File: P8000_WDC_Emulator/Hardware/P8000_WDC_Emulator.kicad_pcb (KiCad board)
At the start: 2 copper layers, 144 x 160.4 mm, 81 parts, among them Q1 CRYSTAL, SW1 SW_PUSH, X1 RS-232, X2 P8000, X3 SD-CON, X4 PATA, X5 4_Pin_Molex, X6 P8000-Compact, X7 AVR-ISP-6

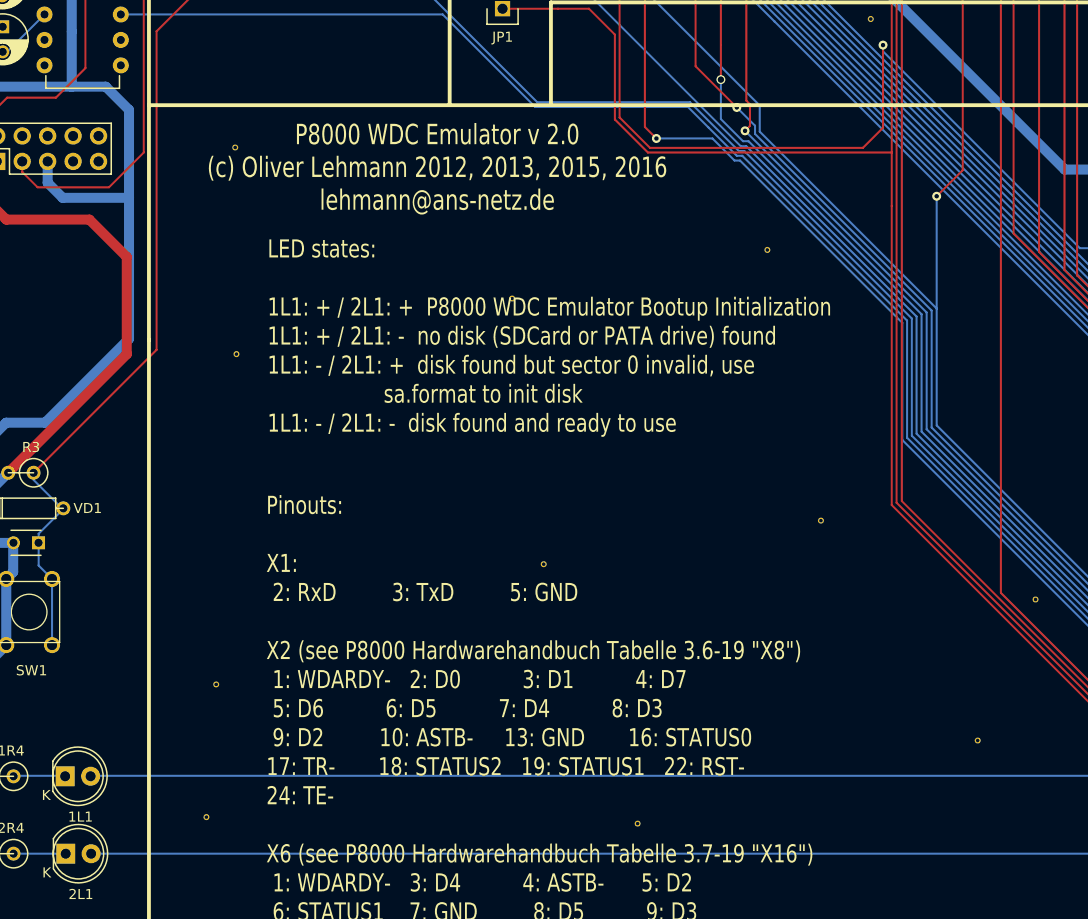
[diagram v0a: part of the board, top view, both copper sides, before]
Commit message: more ground layer
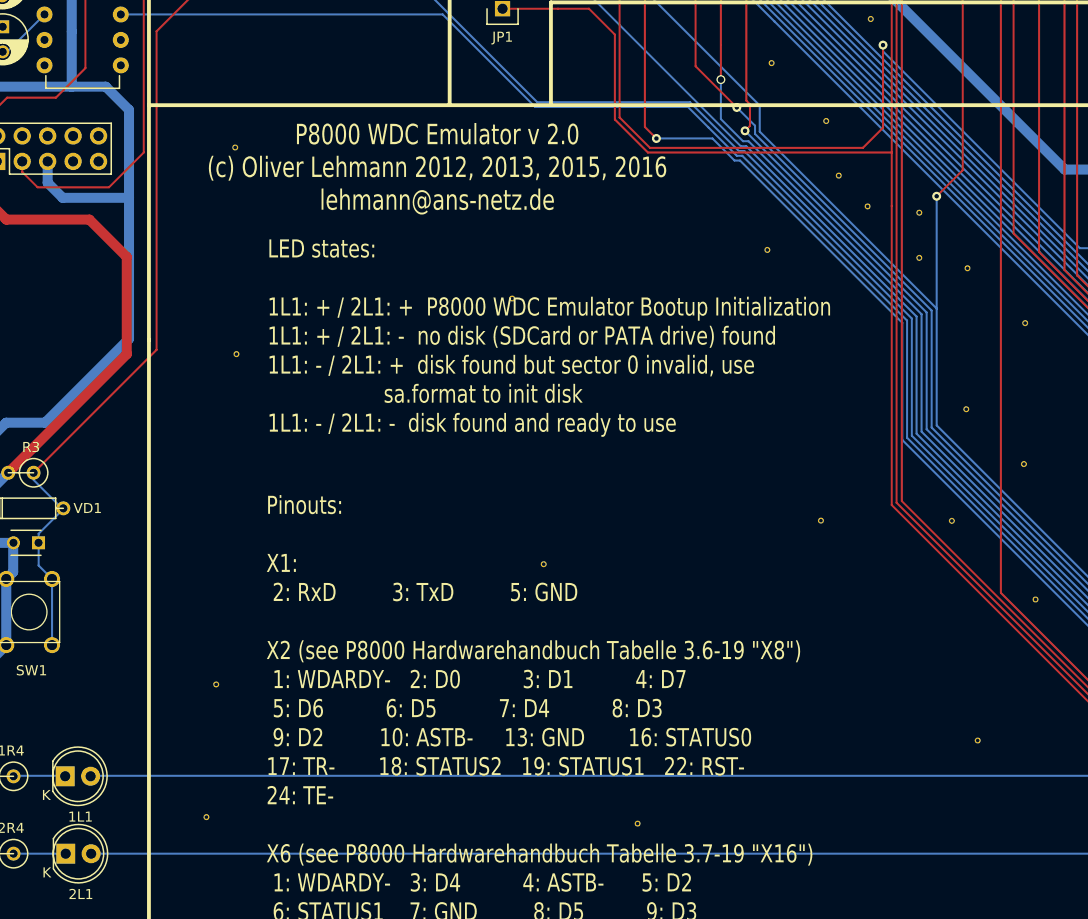
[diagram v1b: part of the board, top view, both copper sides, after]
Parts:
- added VIA-0.6mm: VAL**, Footprints:VIA-0.6mm, F.Cu at (120.6, 112.9)
- added VIA-0.6mm: VAL**, Footprints:VIA-0.6mm, F.Cu at (102.7, 67.2)
- added VIA-0.6mm: VAL**, Footprints:VIA-0.6mm, F.Cu at (109.4, 78.5)
- added VIA-0.6mm: VAL**, Footprints:VIA-0.6mm, F.Cu at (122.2, 87.7)
- added VIA-0.6mm: VAL**, Footprints:VIA-0.6mm, F.Cu at (122.1, 101.8)
- added VIA-0.6mm: VAL**, Footprints:VIA-0.6mm, F.Cu at (127.8, 107.3)
- added VIA-0.6mm: VAL**, Footprints:VIA-0.6mm, F.Cu at (128.0, 93.2)
- added VIA-0.6mm: VAL**, Footprints:VIA-0.6mm, F.Cu at (117.4, 86.7)
- added VIA-0.6mm: VAL**, Footprints:VIA-0.6mm, F.Cu at (117.4, 82.2)
- added VIA-0.6mm: VAL**, Footprints:VIA-0.6mm, F.Cu at (112.2, 81.5)
- added VIA-0.6mm: VAL**, Footprints:VIA-0.6mm, F.Cu at (108.1, 73.0)
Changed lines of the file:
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@@
 (kicad_pcb (version 4) (host pcbnew 4.0.1-stable)
   (general
-    (links 226)
+    (links 237)
     (no_connects 0)
     (area 19.428459 20.282295 164.490038 181.940201)
@@
     (tracks 1219)
     (zones 0)
-    (modules 81)
+    (modules 92)
     (nets 116)
   )
@@
     (mod_text_size 1.524 1.524)
     (mod_text_width 0.3048)
-    (pad_size 1.7272 1.7272)
+    (pad_size 1.9 1.9)
     (pad_drill 1.016)
     (pad_to_mask_clearance 0.254)
@@
     (visible_elements 7FFFFF7F)
     (pcbplotparams
-      (layerselection 0x00030_80000001)
+      (layerselection 0x010e8_80000001)
       (usegerberextensions true)
       (excludeedgelayer false)
@@
       (outputformat 1)
       (mirror false)
-      (drillshape 2)
+      (drillshape 0)
       (scaleselection 1)
       (outputdirectory PCB/))
@@
     (add_net VCC)
   )
+  (module Footprints:VIA-0.6mm (layer Front)
+    (at 120.64492 112.92332)
+    (path VIA-0.6mm)
+    (fp_text reference VIA-0.6mm (at 0 -4.445) (layer F.SilkS) hide
+      (effects (font (thickness 0.3048)))
+    )
+    (fp_text value VAL** (at 0.635 3.81) (layer F.SilkS) hide
+      (effects (font (thickness 0.3048)))
+    )
+    (pad 1 thru_hole circle (at 0 0) (size 0.59944 0.59944) (drill 0.35) (layers *.Cu)
+      (net 41 GND) (clearance 0.00254))
+  )
+  (module Footprints:VIA-0.6mm (layer Front)
+    (at 122.20702 87.7062)
+    (path VIA-0.6mm)
+    (fp_text reference VIA-0.6mm (at 0 -4.445) (layer F.SilkS) hide
+      (effects (font (thickness 0.3048)))
+    )
+    (fp_text value VAL** (at 0.635 3.81) (layer F.SilkS) hide
+      (effects (font (thickness 0.3048)))
+    )
+    (pad 1 thru_hole circle (at 0 0) (size 0.59944 0.59944) (drill 0.35) (layers *.Cu)
+      (net 41 GND) (clearance 0.00254))
+  )
+  (module Footprints:VIA-0.6mm (layer Front)
+    (at 122.08256 101.7778)
+    (path VIA-0.6mm)
+    (fp_text reference VIA-0.6mm (at 0 -4.445) (layer F.SilkS) hide
+      (effects (font (thickness 0.3048)))
+    )
+    (fp_text value VAL** (at 0.635 3.81) (layer F.SilkS) hide
+      (effects (font (thickness 0.3048)))
+    )
+    (pad 1 thru_hole circle (at 0 0) (size 0.59944 0.59944) (drill 0.35) (layers *.Cu)
+      (net 41 GND) (clearance 0.00254))
+  )
+  (module Footprints:VIA-0.6mm (layer Front)
+    (at 127.8382 107.25404)
+    (path VIA-0.6mm)
+    (fp_text reference VIA-0.6mm (at 0 -4.445) (layer F.SilkS) hide
+      (effects (font (thickness 0.3048)))
+    )
+    (fp_text value VAL** (at 0.635 3.81) (layer F.SilkS) hide
+      (effects (font (thickness 0.3048)))
+    )
+    (pad 1 thru_hole circle (at 0 0) (size 0.59944 0.59944) (drill 0.35) (layers *.Cu)
+      (net 41 GND) (clearance 0.00254))
+  )
+  (module Footprints:VIA-0.6mm (layer Front)
+    (at 127.96266 93.18244)
+    (path VIA-0.6mm)
+    (fp_text reference VIA-0.6mm (at 0 -4.445) (layer F.SilkS) hide
+      (effects (font (thickness 0.3048)))
+    )
+    (fp_text value VAL** (at 0.635 3.81) (layer F.SilkS) hide
+      (effects (font (thickness 0.3048)))
+    )
+    (pad 1 thru_hole circle (at 0 0) (size 0.59944 0.59944) (drill 0.35) (layers *.Cu)
+      (net 41 GND) (clearance 0.00254))
+  )
+  (module Footprints:VIA-0.6mm (layer Front)
+    (at 117.39372 86.66988)
+    (path VIA-0.6mm)
+    (fp_text reference VIA-0.6mm (at 0 -4.445) (layer F.SilkS) hide
+      (effects (font (thickness 0.3048)))
+    )
+    (fp_text value VAL** (at 0.635 3.81) (layer F.SilkS) hide
+      (effects (font (thickness 0.3048)))
+    )
+    (pad 1 thru_hole circle (at 0 0) (size 0.59944 0.59944) (drill 0.35) (layers *.Cu)
+      (net 41 GND) (clearance 0.00254))
+  )
+  (module Footprints:VIA-0.6mm (layer Front)
+    (at 117.39372 82.15884)
+    (path VIA-0.6mm)
+    (fp_text reference VIA-0.6mm (at 0 -4.445) (layer F.SilkS) hide
+      (effects (font (thickness 0.3048)))
+    )
+    (fp_text value VAL** (at 0.635 3.81) (layer F.SilkS) hide
+      (effects (font (thickness 0.3048)))
+    )
+    (pad 1 thru_hole circle (at 0 0) (size 0.59944 0.59944) (drill 0.35) (layers *.Cu)
+      (net 41 GND) (clearance 0.00254))
+  )
+  (module Footprints:VIA-0.6mm (layer Front)
+    (at 112.23498 81.52892)
+    (path VIA-0.6mm)
+    (fp_text reference VIA-0.6mm (at 0 -4.445) (layer F.SilkS) hide
+      (effects (font (thickness 0.3048)))
+    )
+    (fp_text value VAL** (at 0.635 3.81) (layer F.SilkS) hide
+      (effects (font (thickness 0.3048)))
+    )
+    (pad 1 thru_hole circle (at 0 0) (size 0.59944 0.59944) (drill 0.35) (layers *.Cu)
+      (net 41 GND) (clearance 0.00254))
+  )
+  (module Footprints:VIA-0.6mm (layer Front)
+    (at 108.09986 73.00722)
+    (path VIA-0.6mm)
+    (fp_text reference VIA-0.6mm (at 0 -4.445) (layer F.SilkS) hide
+      (effects (font (thickness 0.3048)))
+    )
+    (fp_text value VAL** (at 0.635 3.81) (layer F.SilkS) hide
+      (effects (font (thickness 0.3048)))
+    )
+    (pad 1 thru_hole circle (at 0 0) (size 0.59944 0.59944) (drill 0.35) (layers *.Cu)
+      (net 41 GND) (clearance 0.00254))
+  )
+  (module Footprints:VIA-0.6mm (layer Front)
+    (at 102.65156 67.22364)
+    (path VIA-0.6mm)
+    (fp_text reference VIA-0.6mm (at 0 -4.445) (layer F.SilkS) hide
+      (effects (font (thickness 0.3048)))
+    )
+    (fp_text value VAL** (at 0.635 3.81) (layer F.SilkS) hide
+      (effects (font (thickness 0.3048)))
+    )
+    (pad 1 thru_hole circle (at 0 0) (size 0.59944 0.59944) (drill 0.35) (layers *.Cu)
+      (net 41 GND) (clearance 0.00254))
+  )
+  (module Footprints:VIA-0.6mm (layer Front)
+    (at 109.35716 78.45552)
+    (path VIA-0.6mm)
+    (fp_text reference VIA-0.6mm (at 0 -4.445) (layer F.SilkS) hide
+      (effects (font (thickness 0.3048)))
+    )
+    (fp_text value VAL** (at 0.635 3.81) (layer F.SilkS) hide
+      (effects (font (thickness 0.3048)))
+    )
+    (pad 1 thru_hole circle (at 0 0) (size 0.59944 0.59944) (drill 0.35) (layers *.Cu)
+      (net 41 GND) (clearance 0.00254))
+  )
   (module TO92-LM317 (layer Front)
     (at 143.90116 73.12406 270)
@@
       (effects (font (size 1 1) (thickness 0.15)))
     )
-    (pad 1 thru_hole rect (at 0 0 90) (size 2 1.9) (drill 1.00076) (layers *.Cu *.Mask F.SilkS)
+    (pad 1 thru_hole rect (at 0 0 90) (size 2 1.9) (drill 1.016) (layers *.Cu *.Mask F.SilkS)
       (net 52 "Net-(2L1-Pad1)"))
-    (pad 2 thru_hole circle (at 2.54 0) (size 1.9 1.9) (drill 1.00076) (layers *.Cu *.Mask F.SilkS)
+    (pad 2 thru_hole circle (at 2.54 0) (size 1.9 1.9) (drill 1.016) (layers *.Cu *.Mask F.SilkS)
       (net 53 "Net-(2L1-Pad2)"))
     (model LEDs.3dshapes/LED-5MM.wrl
@@
       (effects (font (size 1 1) (thickness 0.15)))
     )
-    (pad 1 thru_hole rect (at 0 0 90) (size 2 1.9) (drill 1.00076) (layers *.Cu *.Mask F.SilkS)
+    (pad 1 thru_hole rect (at 0 0 90) (size 2 1.9) (drill 1.016) (layers *.Cu *.Mask F.SilkS)
       (net 46 "Net-(1L1-Pad1)"))
-    (pad 2 thru_hole circle (at 2.54 0) (size 1.9 1.9) (drill 1.00076) (layers *.Cu *.Mask F.SilkS)
+    (pad 2 thru_hole circle (at 2.54 0) (size 1.9 1.9) (drill 1.016) (layers *.Cu *.Mask F.SilkS)
       (net 47 "Net-(1L1-Pad2)"))
     (model LEDs.3dshapes/LED-5MM.wrl

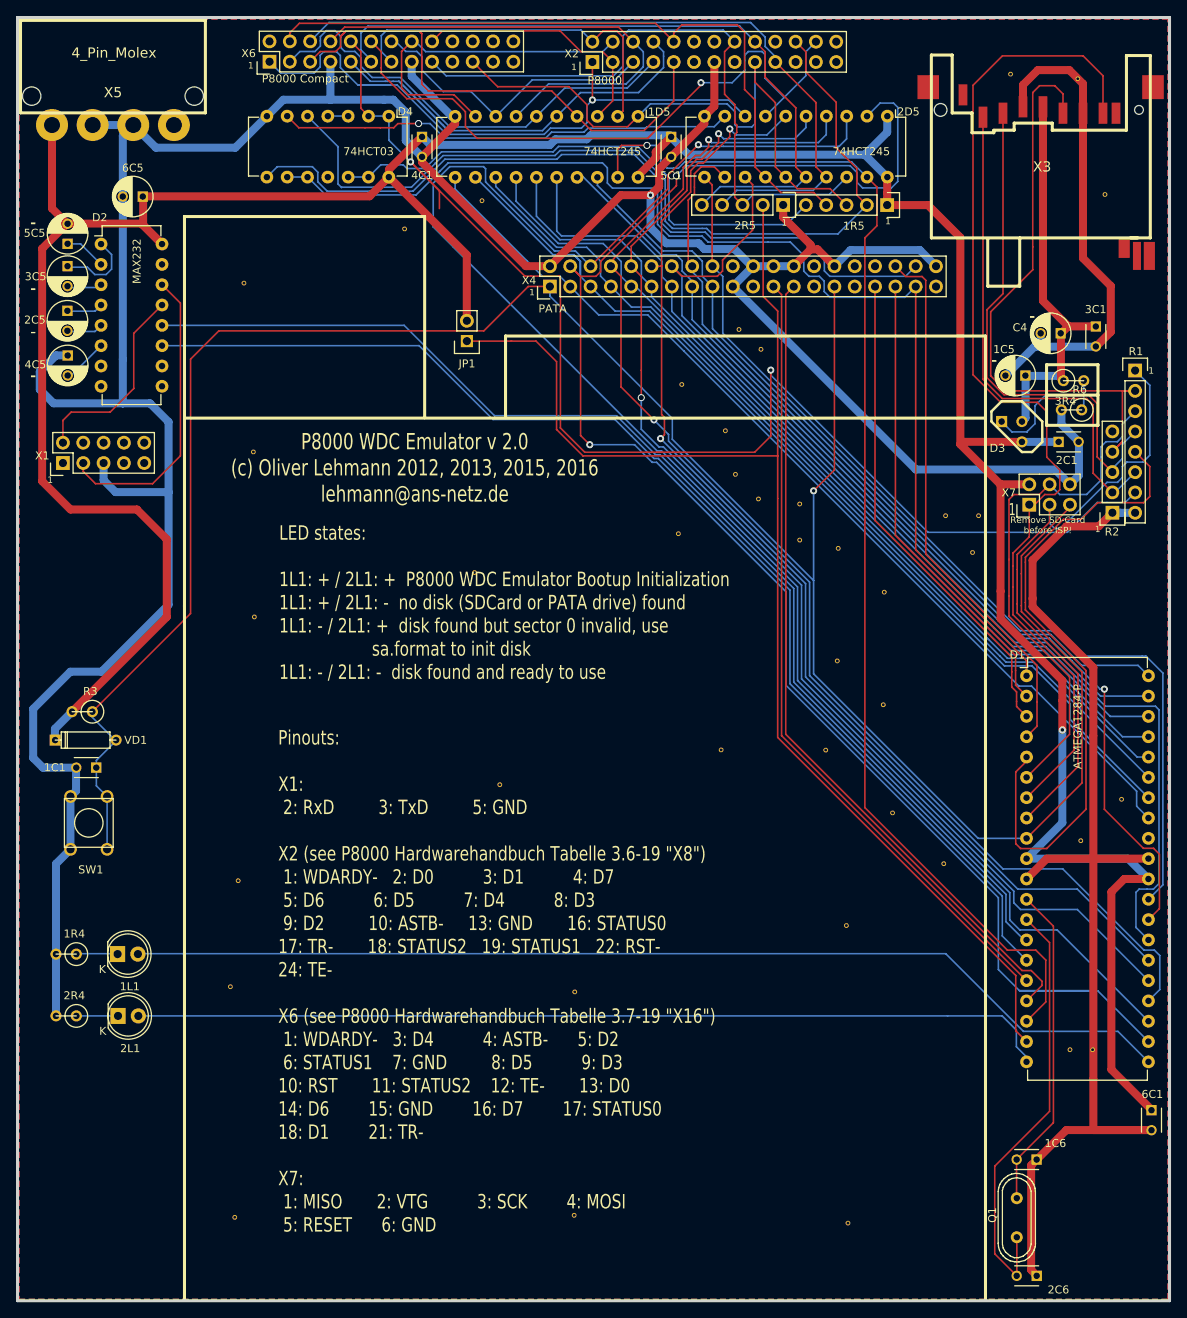
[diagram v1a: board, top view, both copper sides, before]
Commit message: rearrange resistor labels to prevent wrong placement
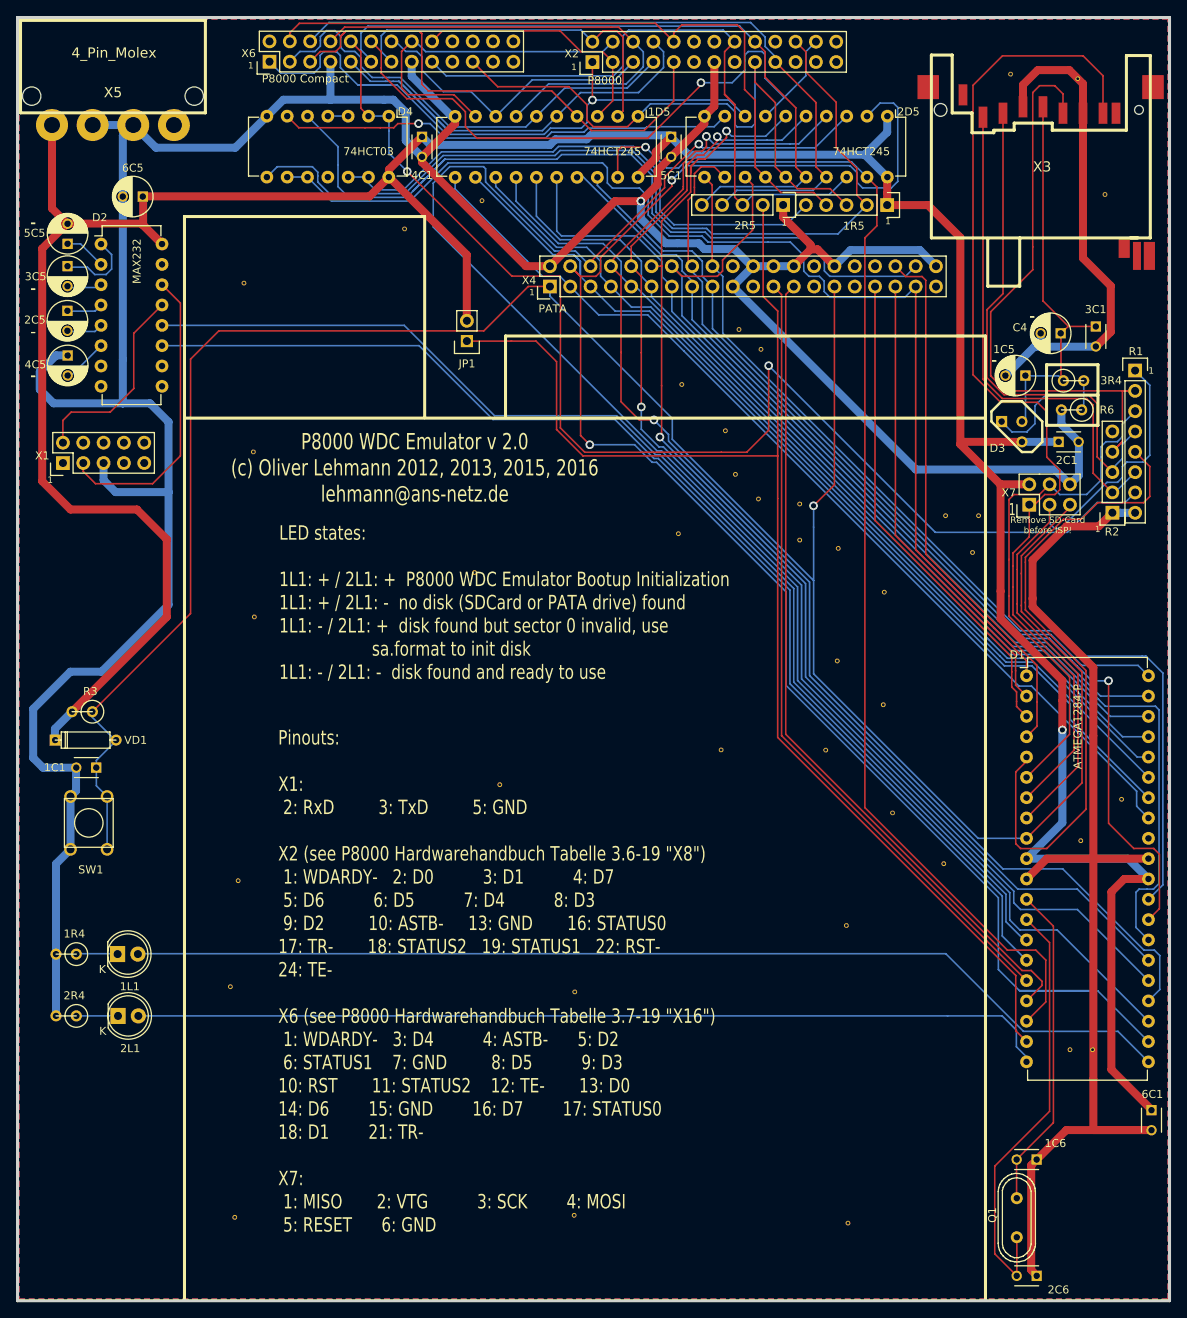
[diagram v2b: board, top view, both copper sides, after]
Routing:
- net /RST1: track 163.5 -> 157.2 mm
- net Net-(D4-Pad8): track 96.2 -> 102.2 mm
- net /PC6: track 126.7 -> 128.3 mm
- net /STATUS0: track 80.3 -> 81.9 mm
- net /PC1: track 214.1 -> 212.8 mm
- net Net-(1D5-Pad19): track 157.4 -> 156.3 mm
- net /PC4: track 147.4 -> 148.5 mm
- net Net-(1R5-Pad5): track 67.3 -> 68.4 mm
- net /PC2: track 165.0 -> 165.7 mm
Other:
- net class 12V: via_dia 0.889 -> 1.08; via_drill 0.635 -> 0.65
- net class 5V: via_dia 0.889 -> 1.08; via_drill 0.635 -> 0.65
- net class Default: via_dia 0.889 -> 1.08; via_drill 0.635 -> 0.65
- net class Power: via_dia 0.889 -> 1.08; via_drill 0.635 -> 0.65
- rule via_min_size: 0.889 -> 1.08
